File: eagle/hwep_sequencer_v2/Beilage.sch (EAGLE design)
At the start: 119 parts, among them X1 ESP32-DEVKIT-C

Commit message: spi test
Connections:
- net ADC088S052_!CS: now also X1.GPIO15/ADC2_CH3/HCS; no longer X1.GPIO21
- net INT_23S08: now also X1.GPIO22
- net STP_!CS: now also X1.GPIO21; no longer X1.GPIO22
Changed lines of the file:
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@@
-</segment>
-</net>
-<net name="ADC088S052_!CS" class="0">
-<segment>
-<wire x1="127" y1="226.06" x2="132.08" y2="226.06" width="0.1524" layer="91"/>
-<label x="132.08" y="226.06" size="1.016" layer="95" font="vector" xref="yes"/>
-<pinref part="X1" gate="G$1" pin="GPIO21"/>
 </segment>
 </net>
@@
 </segment>
 </net>
-<net name="STP_!CS" class="0">
-<segment>
-<pinref part="X1" gate="G$1" pin="GPIO22"/>
-<wire x1="127" y1="233.68" x2="132.08" y2="233.68" width="0.1524" layer="91"/>
-<label x="132.08" y="233.68" size="1.016" layer="95" font="vector" xref="yes"/>
-</segment>
-</net>
 <net name="INT_23S08" class="0">
 <segment>
@@
 <label x="45.72" y="142.24" size="1.016" layer="95" font="vector" rot="R180" xref="yes"/>
 </segment>
+<segment>
+<wire x1="127" y1="233.68" x2="132.08" y2="233.68" width="0.1524" layer="91"/>
+<label x="132.08" y="233.68" size="1.016" layer="95" font="vector" xref="yes"/>
+<pinref part="X1" gate="G$1" pin="GPIO22"/>
+</segment>
 </net>
+<net name="ADC088S052_!CS" class="0">
+<segment>
+<wire x1="127" y1="200.66" x2="132.08" y2="200.66" width="0.1524" layer="91"/>
+<label x="132.08" y="200.66" size="1.016" layer="95" font="vector" xref="yes"/>
+<pinref part="X1" gate="G$1" pin="GPIO15/ADC2_CH3/HCS"/>
+</segment>
+</net>
+<net name="STP_!CS" class="0">
+<segment>
+<wire x1="127" y1="226.06" x2="132.08" y2="226.06" width="0.1524" layer="91"/>
+<label x="132.08" y="226.06" size="1.016" layer="95" font="vector" xref="yes"/>
+<pinref part="X1" gate="G$1" pin="GPIO21"/>
+</segment>
+</net>

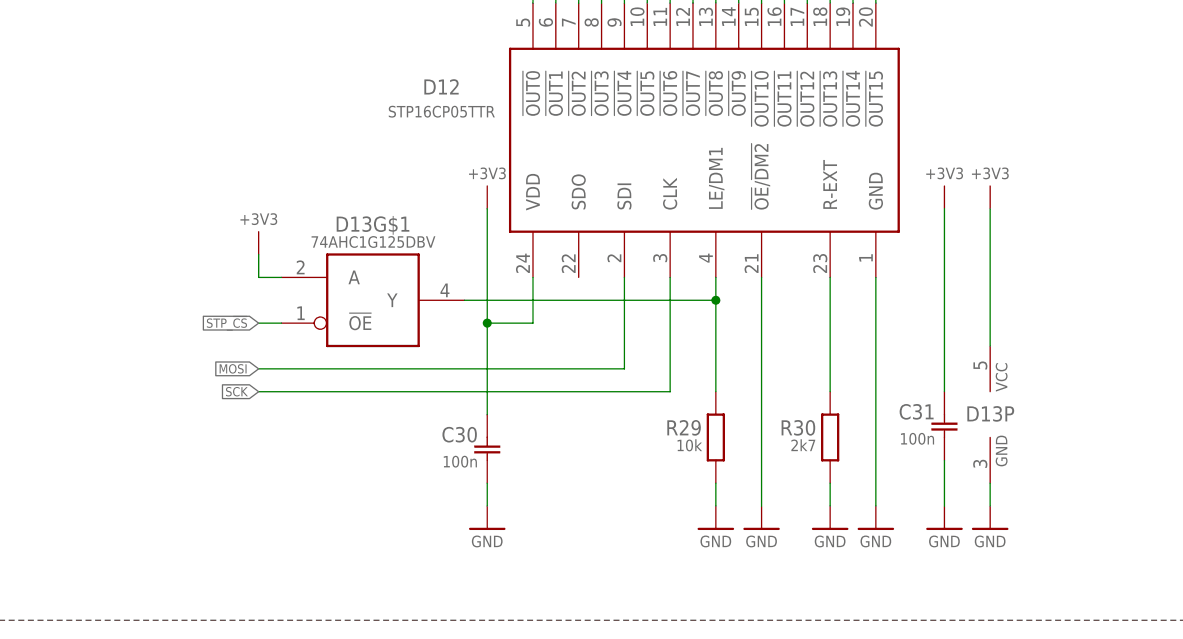
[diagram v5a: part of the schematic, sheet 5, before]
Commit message: mcp23s08 implemented
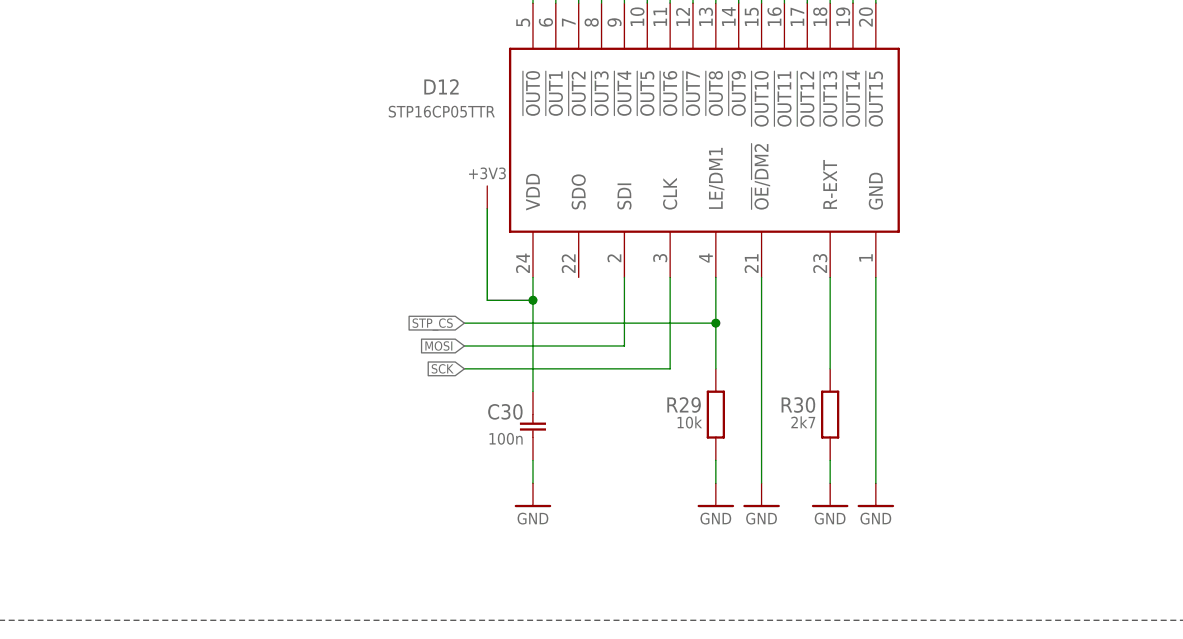
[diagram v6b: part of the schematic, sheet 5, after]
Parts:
- removed C31: 100n, rcl_GruS:C-EUC0805
- removed D13: 74AHC1G125DBV, 74xx_GruS:74AHC1G125DBV
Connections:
- removed net N$61: D12.LE/DM1, D13G$1.Y, R29.2
- removed net STP_!CS: D13G$1.!OE, X1.GPIO21
- new net STP_CS: D12.LE/DM1, R29.2, X1.GPIO21
- net +3V3: no longer C31.1, D13G$1.A, D13P.VCC
- net GND: no longer C31.2, D13P.GND
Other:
- note added: "positive cs"
- moved on the sheet: C30, R29, R30, X2

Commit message: reroute brd complete
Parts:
- X1: value ESP32-DEVKIT-C -> ESP32CLIP2122; device modul_GruS:ESP32-DEVKIT-C -> modul_GruS:ESP32CLIP2122
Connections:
- removed net N$71: H11.DI, H8.DO
- removed net N$8: D9G$1.Y, H3.DI
- new net DI: D9G$1.Y, H11.DI
- new net DO: H14.DO, H3.DI
- net AGND: now also X1.SD1
- net VREF: now also X1.SD0
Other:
- moved on the sheet: D9G$1, X3, X4

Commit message: updated outline
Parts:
- added R27, R28, R31, R32, R33, R34, R35, R36, R37, R38: 18k, rcl_GruS:R-EUSR0805
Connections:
- net DI renamed N$1
- net DO renamed N$2
- net +3V3: now also R27.2, R28.2, R31.2, R32.2, R33.2, R34.2, R35.2, R36.2, R37.2, R38.2
- net EVENT: now also S12.S; no longer S12.S1
- net MOSI: now also D1.SI, D5.DIN
- net PSGS: now also X1.GPIO32/ADC1_CH4
- net Q0_SW_BD: now also R28.1
- net Q0_SW_GD: now also R35.1
- net Q1_SW_BD: now also R31.1
- net Q1_SW_GD: now also R36.1
- net Q2_SW_BD: now also R32.1
- net Q2_SW_GD: now also R37.1
- net Q3_SW_BD: now also R33.1
- net Q3_SW_GD: now also R38.1
- net SRC_SW_BD: now also R27.1
- net SRC_SW_GD: now also R34.1
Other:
- note added: "Internal Pullup"
- note removed: "Internal Weak Pullup"
- moved on the sheet: C1, C10, C3, C9, D1, D2G$1, D2P, D3, D6, D7, D8A, D8B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
